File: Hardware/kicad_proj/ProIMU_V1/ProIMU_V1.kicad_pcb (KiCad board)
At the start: 2 copper layers, 50 x 50 mm, 52 parts, among them J1 Conn_02x03_Counter_Clockwise, J4 502570-0893, U1 ADM101E, U10 STM32F412RETx, U2 ISO1050DUB, U4 AIR602, U5 BMP280, U6 MPU-9250, U7 SPX2920M3-3.3_SOT223, U9 L80-M39

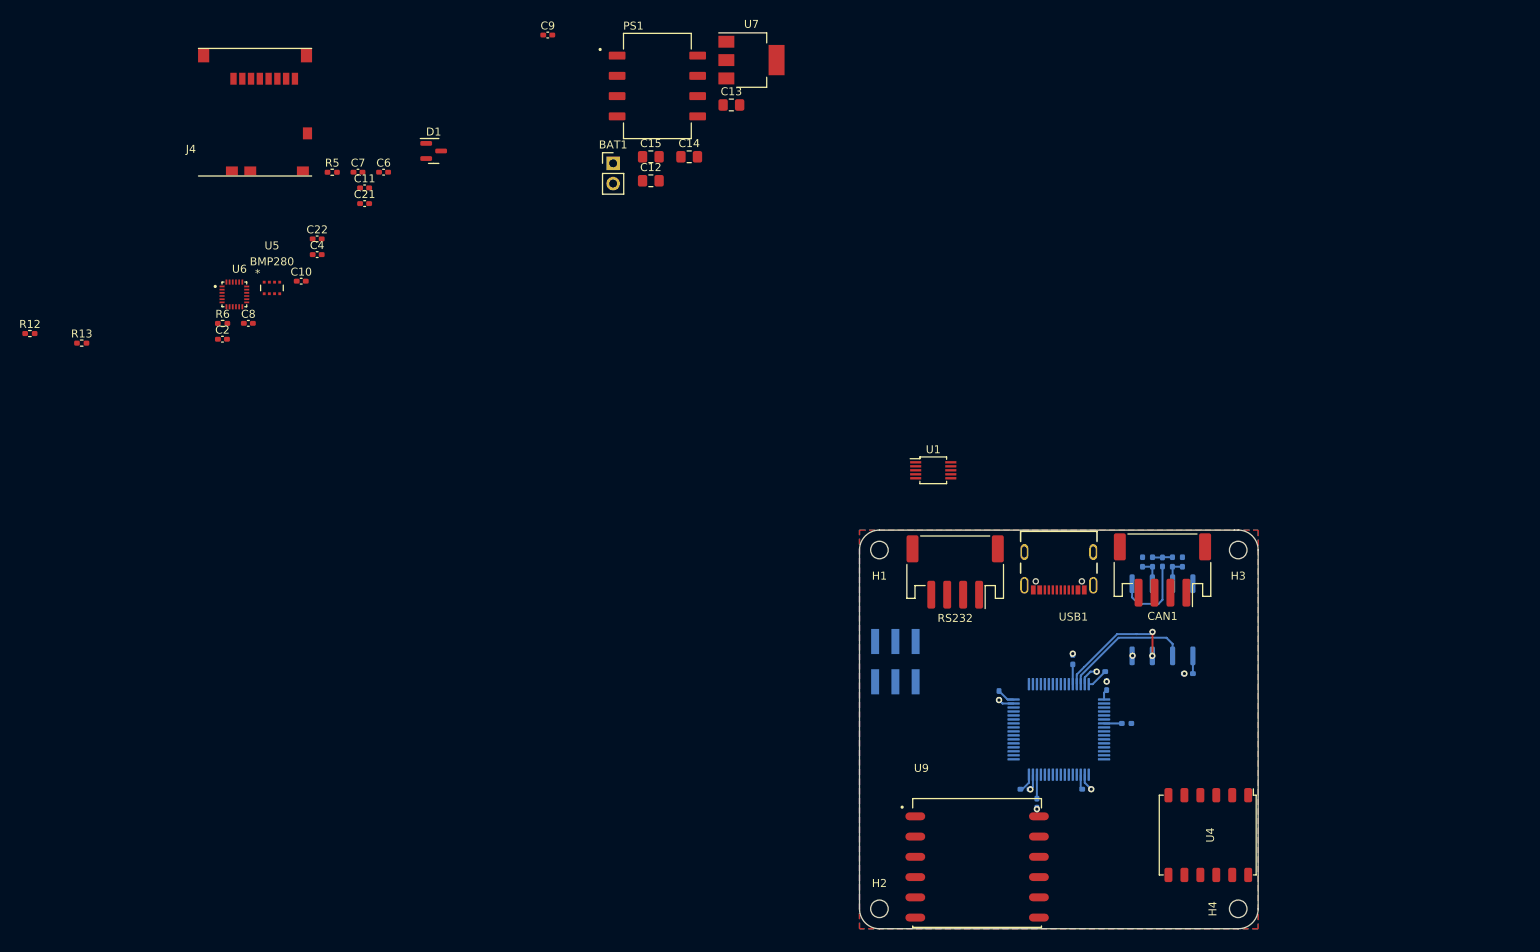
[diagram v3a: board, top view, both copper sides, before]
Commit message: Removed isolated DC-DC converter and added new regulator in place of it
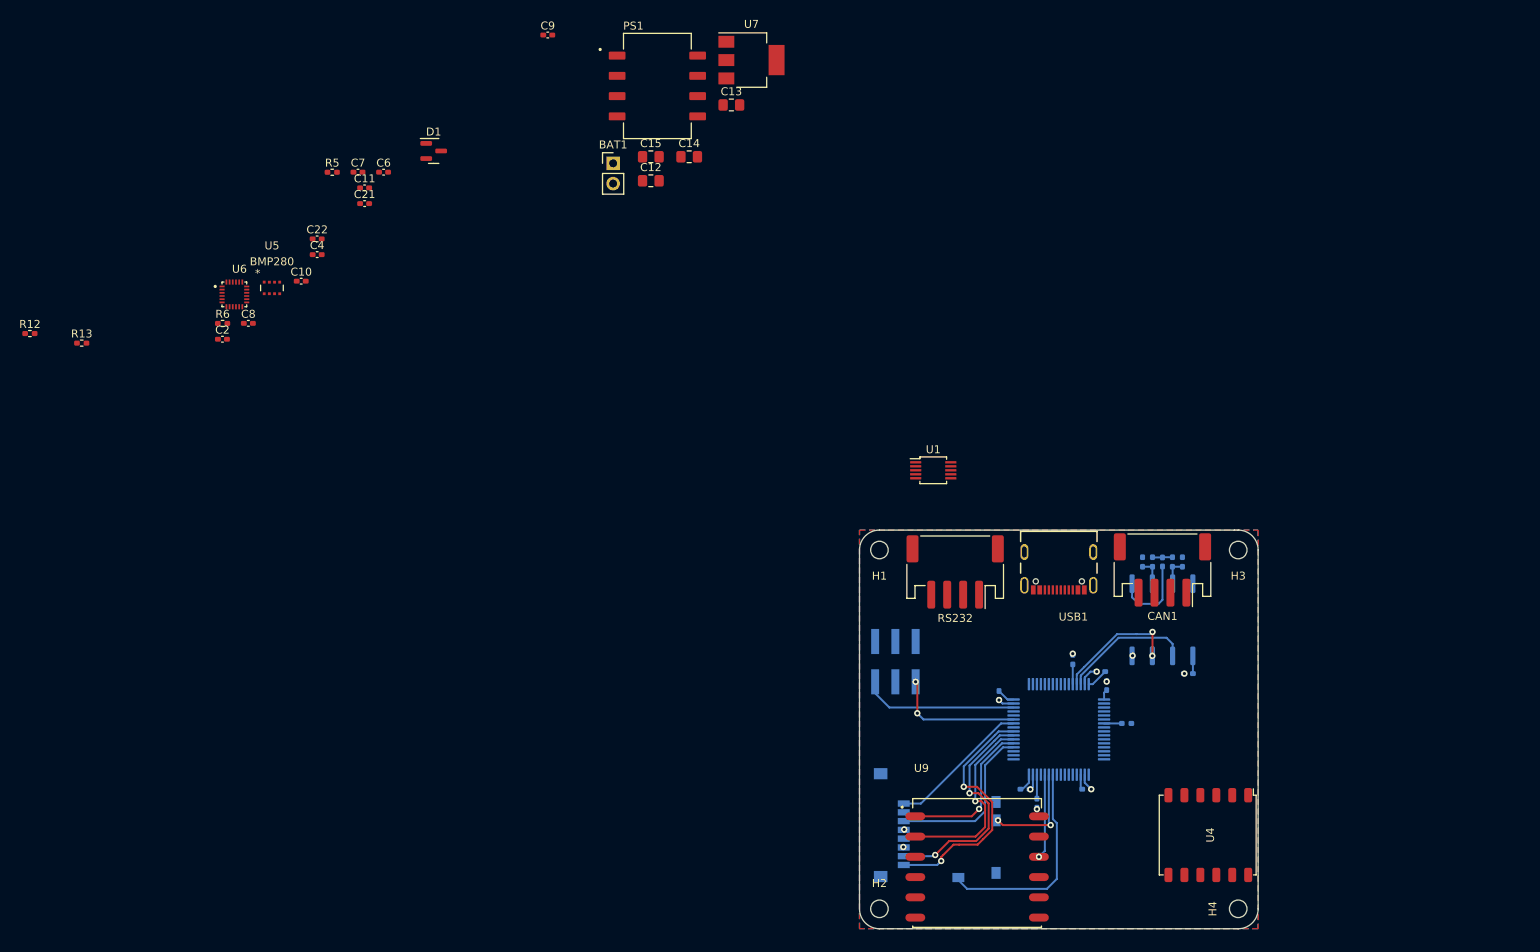
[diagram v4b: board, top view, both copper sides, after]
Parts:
- J4: moved to B.Cu
- moved J4 123.8 mm to (133.2, 117.0), turned to -90 degrees
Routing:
- net /MCU/SDCARD_SDIO_D1: track 0.00 -> 31.7 mm, vias 0 -> 2
- net /MCU/SDCARD_SDIO_D0: track 0.00 -> 28.7 mm, vias 0 -> 2
- net /MCU/SDCARD_DET_LEVEL: track 0.00 -> 26.9 mm
- net /MCU/GPS_UART6_RX: track 0.00 -> 24.1 mm, vias 0 -> 1
- net /MCU/SDCARD_SDIO_CLK: track 0.00 -> 21.0 mm
- net /MCU/DEBUG_SWDIO: track 0.00 -> 19.5 mm
- net /MCU/GPS_UART6_TX: track 0.00 -> 19.3 mm, vias 0 -> 1
- net /MCU/SDCARD_SDIO_D2: track 0.00 -> 17.9 mm
- net /MCU/DEBUG_UART1_RX: track 0.00 -> 16.4 mm, vias 0 -> 2
- net /MCU/SDCARD_DET_SWT: track 0.00 -> 13.3 mm, vias 0 -> 2
- net /MCU/GPS_RESET: track 0.00 -> 10.6 mm, vias 0 -> 1
- net +3V3: track 12.7 -> 12.8 mm, vias 1 -> 2
- net GND: track 9.18 -> 9.25 mm, vias 8 -> 9

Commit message: Updated Schematic and Layout
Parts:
- removed J4: 502570-0893, footprints:MOLEX_502570-0893
- removed PS1: PDP1-S5-S5-M-TR, footprints:CONV_PDP1-S5-S5-M-TR
- removed RS232: Conn_01x04, Connector_JST:JST_PH_S4B-PH-SM4-TB_1x04-1MP_P2.00mm_Horizontal
- added C23: C, Capacitor_SMD:C_0805_2012Metric_Pad1.18x1.45mm_HandSolder, F.Cu at (80.8, 99.2)
- added C24: 4.7uF, Capacitor_SMD:C_0402_1005Metric_Pad0.74x0.62mm_HandSolder, F.Cu at (77.9, 110.0)
- added C25: C, Capacitor_SMD:C_0805_2012Metric_Pad1.18x1.45mm_HandSolder, F.Cu at (80.3, 104.5)
- added C26: 4.7uF, Capacitor_SMD:C_0402_1005Metric_Pad0.74x0.62mm_HandSolder, F.Cu at (84.3, 102.7)
- added C27: C, Capacitor_SMD:C_0805_2012Metric_Pad1.18x1.45mm_HandSolder, F.Cu at (75.5, 104.5)
- added C28: C, Capacitor_SMD:C_0805_2012Metric_Pad1.18x1.45mm_HandSolder, F.Cu at (75.5, 107.5)
- added J2: 502570-0893, footprints:MOLEX_502570-0893, F.Cu at (49.7, 108.4)
- added R10: 2.2K, Resistor_SMD:R_0402_1005Metric_Pad0.72x0.64mm_HandSolder, B.Cu at (143.8, 47.2)
- added R14: 2.2K, Resistor_SMD:R_0402_1005Metric_Pad0.72x0.64mm_HandSolder, F.Cu at (54.7, 124.1)
- added R15: 1K, Resistor_SMD:R_0402_1005Metric_Pad0.72x0.64mm_HandSolder, F.Cu at (84.8, 98.7)
- added R16: 1.18K, Resistor_SMD:R_0402_1005Metric_Pad0.72x0.64mm_HandSolder, F.Cu at (80.0, 101.8)
- added R17: 1.13K, Resistor_SMD:R_0402_1005Metric_Pad0.72x0.64mm_HandSolder, F.Cu at (74.7, 110.0)
- added R18: 1K, Resistor_SMD:R_0402_1005Metric_Pad0.72x0.64mm_HandSolder, F.Cu at (79.5, 107.0)
- added R19: 1K, Resistor_SMD:R_0402_1005Metric_Pad0.72x0.64mm_HandSolder, F.Cu at (84.8, 100.7)
- added R8: 2.2K, Resistor_SMD:R_0402_1005Metric_Pad0.72x0.64mm_HandSolder, B.Cu at (145.5, 46.5)
- added R9: 2.2K, Resistor_SMD:R_0402_1005Metric_Pad0.72x0.64mm_HandSolder, B.Cu at (145.5, 50.8)
- added RS1: Conn_01x04, Connector_JST:JST_PH_S4B-PH-SM4-TB_1x04-1MP_P2.00mm_Horizontal, F.Cu at (90.3, 73.7)
- added U3: L80-M39, footprints:XCVR_L80-M39, F.Cu at (54.1, 80.2)
- added U8: BQ24075RGT, Package_DFN_QFN:VQFN-16-1EP_3x3mm_P0.5mm_EP1.6x1.6mm, F.Cu at (75.7, 100.4)
- C10, C9: value 100nF -> 0.1uF
- C12, C13: value C -> 100nF; footprint Capacitor_SMD:C_0805_2012Metric_Pad1.18x1.45mm_HandSolder -> Capacitor_SMD:C_0402_1005Metric_Pad0.74x0.62mm_HandSolder
- C22: value 1uF -> C; footprint Capacitor_SMD:C_0402_1005Metric_Pad0.74x0.62mm_HandSolder -> Capacitor_SMD:C_0805_2012Metric_Pad1.18x1.45mm_HandSolder
- C3: value 1uF -> 100nF
- C4: moved to B.Cu
- C6: value 100nF -> 1uF
- C7, C8: value 0.1uF -> 1uF
- R1, R2: value 2.2K -> 22R
- R12: value 22R -> 2.2K; moved to B.Cu
- R13: value 22R -> 2.2K
- R4, R5, R7: value 2.2K -> 1K
- R6: value 2.2K -> 1K; moved to B.Cu
- U1: value ADM101E -> ISO1050DUB; footprint Package_SO:MSOP-10_3x3mm_P0.5mm -> Package_SO:SOP-8_6.62x9.15mm_P2.54mm
- U2: value ISO1050DUB -> ADM101E; footprint Package_SO:SOP-8_6.62x9.15mm_P2.54mm -> Package_SO:MSOP-10_3x3mm_P0.5mm
- U5: value BMP280 -> MPU-9250; footprint footprints:BMP280 -> footprints:QFN40P300X300X105-24N
- U6: value MPU-9250 -> BMP280; footprint footprints:QFN40P300X300X105-24N -> footprints:BMP280
- U7: value SPX2920M3-3.3_SOT223 -> TPS63000; footprint Package_TO_SOT_SMD:SOT-223-3_TabPin2 -> Package_SON:Texas_DRC0010J_ThermalVias
- U9: value L80-M39 -> SPX2920M3-3.3_SOT223; footprint footprints:XCVR_L80-M39 -> Package_TO_SOT_SMD:SOT-223-3_TabPin2
- moved R12 124.4 mm to (143.8, 50.2), turned to -90 degrees
- moved C4 90.1 mm to (145.5, 48.8), turned to 180 degrees
- moved R7 67.0 mm to (106.2, 42.8), turned to 90 degrees
- moved R6 64.1 mm to (106.2, 40.2), turned to 90 degrees
- moved U1 25.4 mm to (137.2, 47.5)
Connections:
- net /ANT renamed /Radio/ANT
- C10 pad 1: +3V3 -> Net-(C10-Pad1)
- C12 pad 1: VDD -> +5V
- C12 pad 2: GND1 -> GND
- C13 pad 1: +5V -> +3V3
- C14 pad 1: +5V -> Net-(C14-Pad1)
- C15 pad 1: +3V3 -> Net-(C15-Pad1)
- C2 pad 2: VDD -> Net-(C2-Pad2)
- C21 pad 1: GND2 -> GND
- C21 pad 2: Net-(C21-Pad2) -> VDD
- C22 pad 1: GND2 -> +5V
- C22 pad 2: Net-(C22-Pad2) -> GND
- C3 pad 1: GND1 -> GND
- C3 pad 2: Net-(R1-Pad2) -> +3V3
- C4 pad 1: Net-(C4-Pad1) -> GND1
- C6 pad 1: GND -> Net-(C6-Pad1)
- C6 pad 2: +3V3 -> Net-(C6-Pad2)
- C7 pad 1: +5V -> GND2
- C7 pad 2: GND -> Net-(C7-Pad2)
- C8 pad 1: Net-(C8-Pad1) -> GND2
- C8 pad 2: GND -> Net-(C8-Pad2)
- CAN1 pad 1: VDD -> Net-(CAN1-Pad1)
- D1 pad 1: /MCU/USB- -> /USB /D-
- D1 pad 2: /MCU/USB+ -> /USB /D+
- J1 pad 1: /MCU/DEBUG_UART1_RX -> unconnected-(J1-Pad1)
- J1 pad 2: /MCU/DEBUG_UART1_TX -> unconnected-(J1-Pad2)
- J1 pad 3: /MCU/NRST -> unconnected-(J1-Pad3)
- J1 pad 4: GND -> unconnected-(J1-Pad4)
- J1 pad 5: /MCU/DEBUG_SWDIO -> unconnected-(J1-Pad5)
- J1 pad 6: /MCU/DEBUG_SWCLK -> unconnected-(J1-Pad6)
- R1 pad 2: Net-(R1-Pad2) -> /USB /D+
- R12 pad 1: Net-(R12-Pad1) -> Net-(C4-Pad2)
- R12 pad 2: /MCU/USB+ -> Net-(R12-Pad2)
- R13 pad 1: /MCU/USB- -> Net-(R13-Pad1)
- R13 pad 2: Net-(R13-Pad2) -> +3V3
- R2 pad 1: Net-(R1-Pad2) -> /USB /D-
- R4 pad 1: Net-(CAN1-Pad2) -> /USB /USB_POWER_IND
- R4 pad 2: Net-(R1-Pad1) -> Net-(C2-Pad2)
- R5 pad 1: /MCU/BMP280_I2C1_SDA -> GND
- R5 pad 2: +3V3 -> /USB /USB_POWER_IND
- R6 pad 1: /MCU/BMP280_I2C1_SCL -> /CAN/CAN_POWER_IND
- R6 pad 2: +3V3 -> Net-(CAN1-Pad1)
- R7 pad 1: Net-(CAN1-Pad3) -> GND
- R7 pad 2: Net-(R2-Pad2) -> /CAN/CAN_POWER_IND
- U1 pad 1: GND2 -> +3V3
- U1 pad 2: Net-(C4-Pad1) -> /CAN/CAN1_RX
- U1 pad 3: Net-(C22-Pad2) -> /CAN/CAN1_TX
- U1 pad 4: /MCU/RS232_UART3_TX -> GND
- U1 pad 5: Net-(RS232-Pad4) -> GND1
- U1 pad 6: /MCU/RS232_UART3_RX -> Net-(R12-Pad2)
- U1 pad 8: unconnected-(U1-Pad8) -> VDD
- U2 pad 1: +3V3 -> GND2
- U2 pad 2: /MCU/CAN1_RX -> Net-(C6-Pad1)
- U2 pad 3: /MCU/CAN1_TX -> Net-(C8-Pad2)
- U2 pad 4: GND -> /Isolated UART/UART2_TX
- U2 pad 5: GND1 -> Net-(RS1-Pad4)
- U2 pad 6: Net-(R2-Pad2) -> /Isolated UART/UART2_RX
- U2 pad 7: Net-(R1-Pad1) -> Net-(RS1-Pad3)
- U2 pad 8: VDD -> unconnected-(U2-Pad8)
- U4 pad 12: /MCU/WIFI_RESET -> /Radio/WIFI_RESET
- U4 pad 5: /MCU/WIFI_UART2_RX -> /Radio/WIFI_UART6_RX
- U4 pad 6: /MCU/WIFI_UART2_TX -> /Radio/WIFI_UART6_TX
- U5 pad 1: GND -> +3V3
- U5 pad 2: +3V3 -> (no net)
- U5 pad 3: /MCU/BMP280_I2C1_SDA -> (no net)
- U5 pad 4: /MCU/BMP280_I2C1_SCL -> (no net)
- U5 pad 5: GND -> (no net)
- U5 pad 6: +3V3 -> (no net)
- U5 pad 7: GND -> unconnected-(U5-Pad7)
- U5 pad 8: +5V -> +3V3
- U6 pad 1: +3V3 -> GND
- U6 pad 2: (no net) -> +3V3
- U6 pad 3: (no net) -> Net-(R13-Pad1)
- U6 pad 4: (no net) -> Net-(R14-Pad1)
- U6 pad 5: (no net) -> GND
- U6 pad 6: (no net) -> +3V3
- U6 pad 7: unconnected-(U6-Pad7) -> GND
- U6 pad 8: +3V3 -> +5V
- U7 pad 2: GND -> Net-(L1-Pad2)
- U7 pad 3: +3V3 -> GND
- U9 pad 1: /MCU/GPS_UART6_TX -> +5V
- U9 pad 2: /MCU/GPS_UART6_RX -> GND
- U9 pad 3: GND -> +3V3
- USB1 pad A4_B9: VDD -> Net-(C2-Pad2)
- USB1 pad A6: Net-(R12-Pad1) -> Net-(R1-Pad1)
- USB1 pad A7: Net-(R13-Pad2) -> Net-(R2-Pad2)
- USB1 pad B4_A9: VDD -> Net-(C2-Pad2)
- USB1 pad B6: Net-(R12-Pad1) -> Net-(R1-Pad1)
- USB1 pad B7: Net-(R13-Pad2) -> Net-(R2-Pad2)
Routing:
- net /Isolated UART/UART2_TX: track 0.00 -> 32.3 mm, vias 0 -> 2
- net /MCU/SDCARD_SDIO_D1: track 31.7 -> 0.00 mm, vias 2 -> 0
- net +5V: track 0.00 -> 31.7 mm, vias 0 -> 2
- net /Radio/WIFI_RESET: track 0.00 -> 29.5 mm, vias 0 -> 1
- net unconnected-(J1-Pad5): track 0.00 -> 19.5 mm
- net /MCU/DEBUG_SWDIO: track 19.5 -> 0.00 mm
- net unconnected-(J1-Pad1): track 0.00 -> 16.4 mm, vias 0 -> 2
- net /MCU/DEBUG_UART1_RX: track 16.4 -> 0.00 mm, vias 2 -> 0
- net /MCU/CAN1_RX: track 16.4 -> 0.00 mm
- net /MCU/CAN1_TX: track 15.9 -> 0.00 mm, vias 2 -> 0
- net /Radio/WIFI_UART6_RX: track 0.00 -> 13.9 mm, vias 0 -> 1
- net /Radio/WIFI_UART6_TX: track 0.00 -> 10.8 mm, vias 0 -> 1
- net GND1: track 10.3 -> 0.00 mm
- net GND: track 9.25 -> 19.5 mm
- net Net-(R1-Pad2): track 2.52 -> 0.00 mm
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
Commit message: Updated Schematic and Layout
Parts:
- moved C3 70.5 mm to (96.8, 56.0)
- moved C5 70.5 mm to (100.0, 70.0)
- moved R1 70.5 mm to (98.0, 56.0)
- moved R2 70.5 mm to (95.5, 56.0)
- moved R4 70.5 mm to (99.2, 56.0)
- moved U2 70.5 mm to (96.8, 63.2)
- moved RS1 68.8 mm to (154.5, 49.0), turned to 90 degrees
- moved U1 54.7 mm to (161.5, 96.5), turned to 90 degrees
- moved R10 46.2 mm to (161.2, 90.0), turned to 0 degrees
- moved R12 44.7 mm to (164.2, 90.0), turned to 0 degrees
- moved R8 44.4 mm to (160.5, 88.2), turned to -90 degrees
- moved C4 43.1 mm to (162.8, 88.2), turned to -90 degrees
- moved R9 42.2 mm to (164.8, 88.2), turned to -90 degrees
- moved CAN1 0.35 mm to (161.8, 85.2)
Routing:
- net /Isolated UART/UART2_TX: track 32.3 -> 0.00 mm, vias 2 -> 0
- net +5V: track 31.7 -> 0.00 mm, vias 2 -> 0
- net /Radio/WIFI_RESET: track 29.5 -> 0.00 mm, vias 1 -> 0
- net /MCU/SDCARD_SDIO_D0: track 28.7 -> 0.00 mm, vias 2 -> 0
- net /MCU/SDCARD_DET_LEVEL: track 26.9 -> 0.00 mm
- net /MCU/GPS_UART6_RX: track 24.1 -> 0.00 mm, vias 1 -> 0
- net /MCU/SDCARD_SDIO_CLK: track 21.0 -> 0.00 mm
- net unconnected-(J1-Pad5): track 19.5 -> 0.00 mm
- net GND: track 19.5 -> 0.00 mm, vias 9 -> 0
- net /MCU/GPS_UART6_TX: track 19.3 -> 0.00 mm, vias 1 -> 0
- net /MCU/SDCARD_SDIO_D2: track 17.9 -> 0.00 mm
- net unconnected-(J1-Pad1): track 16.4 -> 0.00 mm, vias 2 -> 0
- net +3V3: track 15.3 -> 0.00 mm, vias 2 -> 0
- net /Radio/WIFI_UART6_RX: track 13.9 -> 0.00 mm, vias 1 -> 0
- net /MCU/SDCARD_DET_SWT: track 13.3 -> 0.00 mm, vias 2 -> 0
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
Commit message: Updated Repo
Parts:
- removed C24, C26: 4.7uF, Capacitor_SMD:C_0402_1005Metric_Pad0.74x0.62mm_HandSolder
- removed C25, C27, C28: C, Capacitor_SMD:C_0805_2012Metric_Pad1.18x1.45mm_HandSolder
- removed CAN1, RS1: Conn_01x04, Connector_JST:JST_PH_S4B-PH-SM4-TB_1x04-1MP_P2.00mm_Horizontal
- removed R12, R13, R14: 2.2K, Resistor_SMD:R_0402_1005Metric_Pad0.72x0.64mm_HandSolder
- removed R15, R18, R19: 1K, Resistor_SMD:R_0402_1005Metric_Pad0.72x0.64mm_HandSolder
- removed R16: 1.18K, Resistor_SMD:R_0402_1005Metric_Pad0.72x0.64mm_HandSolder
- removed R17: 1.13K, Resistor_SMD:R_0402_1005Metric_Pad0.72x0.64mm_HandSolder
- removed U10: STM32F412RETx, Package_QFP:LQFP-64_10x10mm_P0.5mm
- removed U9: SPX2920M3-3.3_SOT223, Package_TO_SOT_SMD:SOT-223-3_TabPin2
- C1: value 1uF -> 10nF
- C10, C9: value 0.1uF -> 1uF
- C11: value 10nF -> 1uF
- C12, C13: value 100nF -> 1uF
- C17, C18, C20: value 1uF -> C; footprint Capacitor_SMD:C_0402_1005Metric_Pad0.74x0.62mm_HandSolder -> Capacitor_SMD:C_0805_2012Metric_Pad1.18x1.45mm_HandSolder
- C19, C21: value 1uF -> 4.7uF
- C2: value 1uF -> 100nF
- C4, C5: value 1uF -> 0.1uF
- R1, R2: value 22R -> 2.2K
- R10: value 2.2K -> 1K
- R11: value 10K -> 1K
- R4: value 1K -> 10K
- R5, R6: value 1K -> 22R
- R8: value 2.2K -> 1.18K
- R9: value 2.2K -> 1.13K
- U1: value ISO1050DUB -> MPU-9250; footprint Package_SO:SOP-8_6.62x9.15mm_P2.54mm -> footprints:QFN40P300X300X105-24N
- U2: value ADM101E -> BMP280; footprint Package_SO:MSOP-10_3x3mm_P0.5mm -> footprints:BMP280
- U3: value L80-M39 -> STM32F411CEUx; footprint footprints:XCVR_L80-M39 -> Package_DFN_QFN:QFN-48-1EP_7x7mm_P0.5mm_EP5.6x5.6mm
- U4: value AIR602 -> L80-M39; footprint footprints:AIR602 -> footprints:XCVR_L80-M39; moved to B.Cu
- U5: value MPU-9250 -> AIR602; footprint footprints:QFN40P300X300X105-24N -> footprints:AIR602
- U6: value BMP280 -> TPS63000; footprint footprints:BMP280 -> Package_SON:Texas_DRC0010J_ThermalVias
- U7: value TPS63000 -> BQ24075RGT; footprint Package_SON:Texas_DRC0010J_ThermalVias -> Package_DFN_QFN:VQFN-16-1EP_3x3mm_P0.5mm_EP1.6x1.6mm
- U8: value BQ24075RGT -> SPX2920M3-3.3_SOT223; footprint Package_DFN_QFN:VQFN-16-1EP_3x3mm_P0.5mm_EP1.6x1.6mm -> Package_TO_SOT_SMD:SOT-223-3_TabPin2
- moved U3 60.5 mm to (92.5, 127.0)
- moved U1 31.1 mm to (184.5, 75.5)
- moved U4 0.35 mm to (167.0, 118.5), turned to 90 degrees
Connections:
- C10 pad 1: Net-(C10-Pad1) -> +3V3
- C12 pad 1: +5V -> +3V3
- C13 pad 1: +3V3 -> GND
- C13 pad 2: GND -> Net-(C13-Pad2)
- C16 pad 1: Net-(C16-Pad1) -> GND
- C16 pad 2: GND -> VDD
- C17 pad 1: +3V3 -> +5V
- C18 pad 1: +3V3 -> +5V
- C19 pad 1: +3V3 -> GND
- C19 pad 2: GND -> VCC
- C2 pad 1: GND -> +5V
- C2 pad 2: Net-(C2-Pad2) -> GND
- C20 pad 1: +3V3 -> +5V
- C21 pad 2: VDD -> Net-(BAT1-Pad1)
- C23 pad 1: +5V -> +3V3
- C3 pad 1: GND -> +3V3
- C3 pad 2: +3V3 -> GND
- C4 pad 1: GND1 -> Net-(C4-Pad1)
- C4 pad 2: Net-(C4-Pad2) -> GND
- C5 pad 1: GND -> +5V
- C5 pad 2: +3V3 -> GND
- C6 pad 2: Net-(C6-Pad2) -> GND
- C7 pad 1: GND2 -> +3V3
- C7 pad 2: Net-(C7-Pad2) -> GND
- C8 pad 1: GND2 -> +3V3
- C8 pad 2: Net-(C8-Pad2) -> GND
- C9 pad 1: +5V -> +3V3
- D1 pad 1: /USB /D- -> Net-(D1-Pad1)
- D1 pad 2: /USB /D+ -> Net-(D1-Pad2)
- J1 pad 1: unconnected-(J1-Pad1) -> /NRST
- J1 pad 2: unconnected-(J1-Pad2) -> Net-(J1-Pad2)
- J1 pad 3: unconnected-(J1-Pad3) -> Net-(J1-Pad3)
- J2 pad 1: unconnected-(J2-Pad1) -> Net-(J2-Pad1)
- J2 pad 2: unconnected-(J2-Pad2) -> /SDIO_D3
- J2 pad 3: unconnected-(J2-Pad3) -> Net-(J2-Pad3)
- J2 pad 5: unconnected-(J2-Pad5) -> /SDIO_CK
- J2 pad 7: unconnected-(J2-Pad7) -> /SDIO_D0
- J2 pad 8: unconnected-(J2-Pad8) -> Net-(J2-Pad8)
- J2 pad DL: unconnected-(J2-PadDL) -> Net-(J2-PadDL)
- J2 pad DS: unconnected-(J2-PadDS) -> Net-(J2-PadDS)
- R1 pad 1: Net-(R1-Pad1) -> /I2C2_SDA
- R1 pad 2: /USB /D+ -> +3V3
- R10 pad 1: Net-(R10-Pad1) -> Net-(D2-Pad2)
- R10 pad 2: Net-(C4-Pad2) -> VCC
- R11 pad 1: +3V3 -> Net-(D3-Pad2)
- R11 pad 2: Net-(R11-Pad2) -> VCC
- R2 pad 1: /USB /D- -> Net-(R2-Pad1)
- R2 pad 2: Net-(R2-Pad2) -> +3V3
- R3 pad 1: /MCU/NRST -> +3V3
- R3 pad 2: +3V3 -> Net-(R3-Pad2)
- R4 pad 1: /USB /USB_POWER_IND -> /NRST
- R4 pad 2: Net-(C2-Pad2) -> +3V3
- R5 pad 1: GND -> Net-(R5-Pad1)
- R5 pad 2: /USB /USB_POWER_IND -> Net-(D1-Pad2)
- R6 pad 1: /CAN/CAN_POWER_IND -> Net-(D1-Pad1)
- R6 pad 2: Net-(CAN1-Pad1) -> Net-(R6-Pad2)
- R7 pad 1: GND -> Net-(C15-Pad1)
- R7 pad 2: /CAN/CAN_POWER_IND -> Net-(C14-Pad1)
- R8 pad 1: Net-(CAN1-Pad2) -> GND
- R8 pad 2: Net-(R10-Pad1) -> Net-(R8-Pad2)
- R9 pad 1: Net-(CAN1-Pad3) -> GND
- R9 pad 2: Net-(R12-Pad2) -> Net-(R9-Pad2)
- U1 pad 2: /CAN/CAN1_RX -> (no net)
- U1 pad 3: /CAN/CAN1_TX -> (no net)
- U1 pad 4: GND -> (no net)
- U1 pad 5: GND1 -> (no net)
- U1 pad 6: Net-(R12-Pad2) -> (no net)
- U1 pad 7: Net-(R10-Pad1) -> unconnected-(U1-Pad7)
- U1 pad 8: VDD -> +3V3
- U2 pad 1: GND2 -> GND
- U2 pad 2: Net-(C6-Pad1) -> +3V3
- U2 pad 3: Net-(C8-Pad2) -> /I2C2_SDA
- U2 pad 4: /Isolated UART/UART2_TX -> Net-(R2-Pad1)
- U2 pad 5: Net-(RS1-Pad4) -> GND
- U2 pad 6: /Isolated UART/UART2_RX -> +3V3
- U2 pad 7: Net-(RS1-Pad3) -> GND
- U2 pad 8: unconnected-(U2-Pad8) -> +5V
- U3 pad 1: /Radio/GPS_UART3_TX -> +3V3
- U3 pad 10: /Radio/GPS_RESET -> unconnected-(U3-Pad10)
- U3 pad 12: GND -> Net-(U3-Pad12)
- U3 pad 2: /Radio/GPS_UART3_RX -> unconnected-(U3-Pad2)
- U3 pad 3: GND -> unconnected-(U3-Pad3)
- U3 pad 4: +3V3 -> unconnected-(U3-Pad4)
- U3 pad 5: +3V3 -> unconnected-(U3-Pad5)
- U3 pad 7: unconnected-(U3-Pad7) -> /NRST
- U3 pad 8: unconnected-(U3-Pad8) -> GND
- U3 pad 9: (no net) -> +3V3
- U4 pad 1: GND -> Net-(U3-Pad38)
- U4 pad 12: /Radio/WIFI_RESET -> GND
- U4 pad 2: /Radio/ANT -> Net-(U3-Pad31)
- U4 pad 5: /Radio/WIFI_UART6_RX -> +3V3
- U4 pad 6: /Radio/WIFI_UART6_TX -> unconnected-(U4-Pad6)
- U4 pad 9: unconnected-(U4-Pad9) -> (no net)
- U5 pad 1: +3V3 -> GND
- U5 pad 10: Net-(C10-Pad1) -> unconnected-(U5-Pad10)
- U5 pad 12: unconnected-(U5-Pad12) -> Net-(U3-Pad14)
- U5 pad 2: (no net) -> /ANT
- U5 pad 3: (no net) -> GND
- U5 pad 4: (no net) -> +3V3
- U5 pad 5: (no net) -> Net-(U3-Pad13)
- U5 pad 6: (no net) -> Net-(U3-Pad12)
- U5 pad 8: +3V3 -> unconnected-(U5-Pad8)
- U6 pad 1: GND -> +5V
- U6 pad 2: +3V3 -> Net-(L1-Pad2)
- U6 pad 3: Net-(R13-Pad1) -> GND
- U6 pad 5: GND -> Net-(C14-Pad1)
- U6 pad 6: +3V3 -> Net-(C15-Pad1)
- U6 pad 7: GND -> Net-(C15-Pad1)
- U6 pad 8: +5V -> Net-(C15-Pad1)
- U7 pad 1: +5V -> Net-(BAT1-Pad2)
- U7 pad 10: +5V -> VCC
- U7 pad 11: GND -> VCC
- U7 pad 2: Net-(L1-Pad2) -> Net-(BAT1-Pad1)
- U7 pad 3: GND -> Net-(BAT1-Pad1)
- U7 pad 4: Net-(L1-Pad1) (its old number) -> unconnected-(U7-Pad4)
- U7 pad 5: Net-(C14-Pad1) -> VCC
- U7 pad 6: Net-(C15-Pad1) -> VCC
- U7 pad 7: Net-(C15-Pad1) -> Net-(D2-Pad1)
- U7 pad 8: Net-(C15-Pad1) -> GND
- U7 pad 9: GND -> Net-(D3-Pad1)
- U8 pad 1: Net-(BAT1-Pad2) -> +5V
- U8 pad 2: Net-(BAT1-Pad1) -> GND
- U8 pad 3: Net-(BAT1-Pad1) -> +3V3
- USB1 pad A4_B9: Net-(C2-Pad2) -> Net-(C13-Pad2)
- USB1 pad A6: Net-(R1-Pad1) -> Net-(R5-Pad1)
- USB1 pad A7: Net-(R2-Pad2) -> Net-(R6-Pad2)
- USB1 pad B4_A9: Net-(C2-Pad2) -> Net-(C13-Pad2)
- USB1 pad B6: Net-(R1-Pad1) -> Net-(R5-Pad1)
- USB1 pad B7: Net-(R2-Pad2) -> Net-(R6-Pad2)

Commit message: Updated Schematic and Layout
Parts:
- C1, C4, C5, U4: moved to F.Cu
- C10, C11, C6, C7, C8, C9, U3: moved to B.Cu
- moved C7 117.9 mm to (153.3, 108.0), turned to 90 degrees
- moved C8 116.9 mm to (153.8, 101.3)
- moved C11 111.1 mm to (145.5, 109.7)
- moved C6 108.9 mm to (151.2, 100.1)
- moved C10 107.9 mm to (143.7, 108.0), turned to -90 degrees
- moved C9 102.9 mm to (142.2, 103.0), turned to -90 degrees
- moved C17 101.8 mm to (41.6, 78.7)
- moved J2 99.7 mm to (148.4, 122.0)
- moved C16 98.0 mm to (51.9, 86.3)
- moved C18 98.0 mm to (50.4, 84.6)
- moved C19 98.0 mm to (58.1, 84.6)
- moved R4 65.3 mm to (142.8, 104.7), turned to 180 degrees
- moved U3 60.2 mm to (148.5, 105.0)
- moved C5 57.0 mm to (145.7, 104.0), turned to 90 degrees
- moved C20 47.8 mm to (196.0, 75.7)
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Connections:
- J2 pad DL: Net-(J2-PadDL) -> /SD_DET_LEVEL
- U3 pad 17: Net-(J2-PadDL) -> unconnected-(U3-Pad17)
- U3 pad 45: unconnected-(U3-Pad45) -> /SD_DET_LEVEL
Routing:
- net /SDIO_CK: track 0.00 -> 35.4 mm, vias 0 -> 1
- net Net-(J2-Pad1): track 0.00 -> 34.6 mm, vias 0 -> 1
- net Net-(J2-Pad3): track 0.00 -> 27.7 mm, vias 0 -> 1
- net /SD_DET_LEVEL: track 0.00 -> 26.7 mm, vias 0 -> 1
- net Net-(J2-Pad8): track 0.00 -> 24.7 mm, vias 0 -> 1
- net +3V3: track 0.00 -> 11.7 mm
- net /SDIO_D3: track 0.00 -> 10.4 mm, vias 0 -> 1
- net GND: track 0.00 -> 7.86 mm, vias 0 -> 1
- net Net-(R3-Pad2): track 0.00 -> 2.19 mm
- net /NRST: track 0.00 -> 1.69 mm
- net Net-(C6-Pad1): track 0.00 -> 1.62 mm
- net +5V: track 0.00 -> 1.49 mm
- net Net-(C4-Pad1): track 0.00 -> 1.45 mm
